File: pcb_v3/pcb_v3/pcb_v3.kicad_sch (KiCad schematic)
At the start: 21 parts, among them J1 Conn_01x05_Socket, J2 Conn_01x04_Pin, J3 Conn_01x04_Socket, U10 TCRT5000, U11 TCRT5000, U2 ULN2003A, U3 NODEMCU-32S, U4 TCRT5000, U5 TCRT5000, U6 TCRT5000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

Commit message: done all footprint
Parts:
- J2: footprint (none) -> Connector_PinHeader_2.54mm:PinHeader_1x04_P2.54mm_Vertical
- J3: footprint (none) -> Connector_PinSocket_2.54mm:PinSocket_1x04_P2.54mm_Vertical
- U2: footprint (none) -> Package_DIP:DIP-16_W7.62mm
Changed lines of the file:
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@@
 			)
 		)
-		(property "Footprint" ""
+		(property "Footprint" "Connector_PinSocket_2.54mm:PinSocket_1x04_P2.54mm_Vertical"
 			(at 99.06 38.1 0)
 			(hide yes)
@@
 			)
 		)
-		(property "Footprint" ""
+		(property "Footprint" "Package_DIP:DIP-16_W7.62mm"
 			(at 54.61 184.15 0)
 			(hide yes)
@@
 			)
 		)
-		(property "Footprint" ""
+		(property "Footprint" "Connector_PinHeader_2.54mm:PinHeader_1x04_P2.54mm_Vertical"
 			(at 121.92 116.84 0)
 			(hide yes)

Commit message: wrong tcrt wiring
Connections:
- net R_U10: now also U10.A; no longer U10.COLL
- net R_U11: now also U11.A; no longer U11.COLL
- net R_U4: now also U4.A; no longer U4.COLL
- net R_U5: now also U5.A; no longer U5.COLL
- net R_U6: now also U6.A; no longer U6.COLL
- net R_U7: now also U7.A; no longer U7.COLL
- net R_U8: now also U8.A; no longer U8.COLL
- net R_U9: now also U9.A; no longer U9.COLL
- net U10_MUXc6: now also U10.COLL; no longer U10.A
- net U11_MUXc7: now also U11.COLL; no longer U11.A
- net U4_MUXc0: now also U4.COLL; no longer U4.A
- net U5_MUXc1: now also U5.COLL; no longer U5.A
- net U6_MUXc2: now also U6.COLL; no longer U6.A
- net U7_MUXc3: now also U7.COLL; no longer U7.A
- net U8_MUXc4: now also U8.COLL; no longer U8.A
- net U9_MUXc5: now also U9.COLL; no longer U9.A

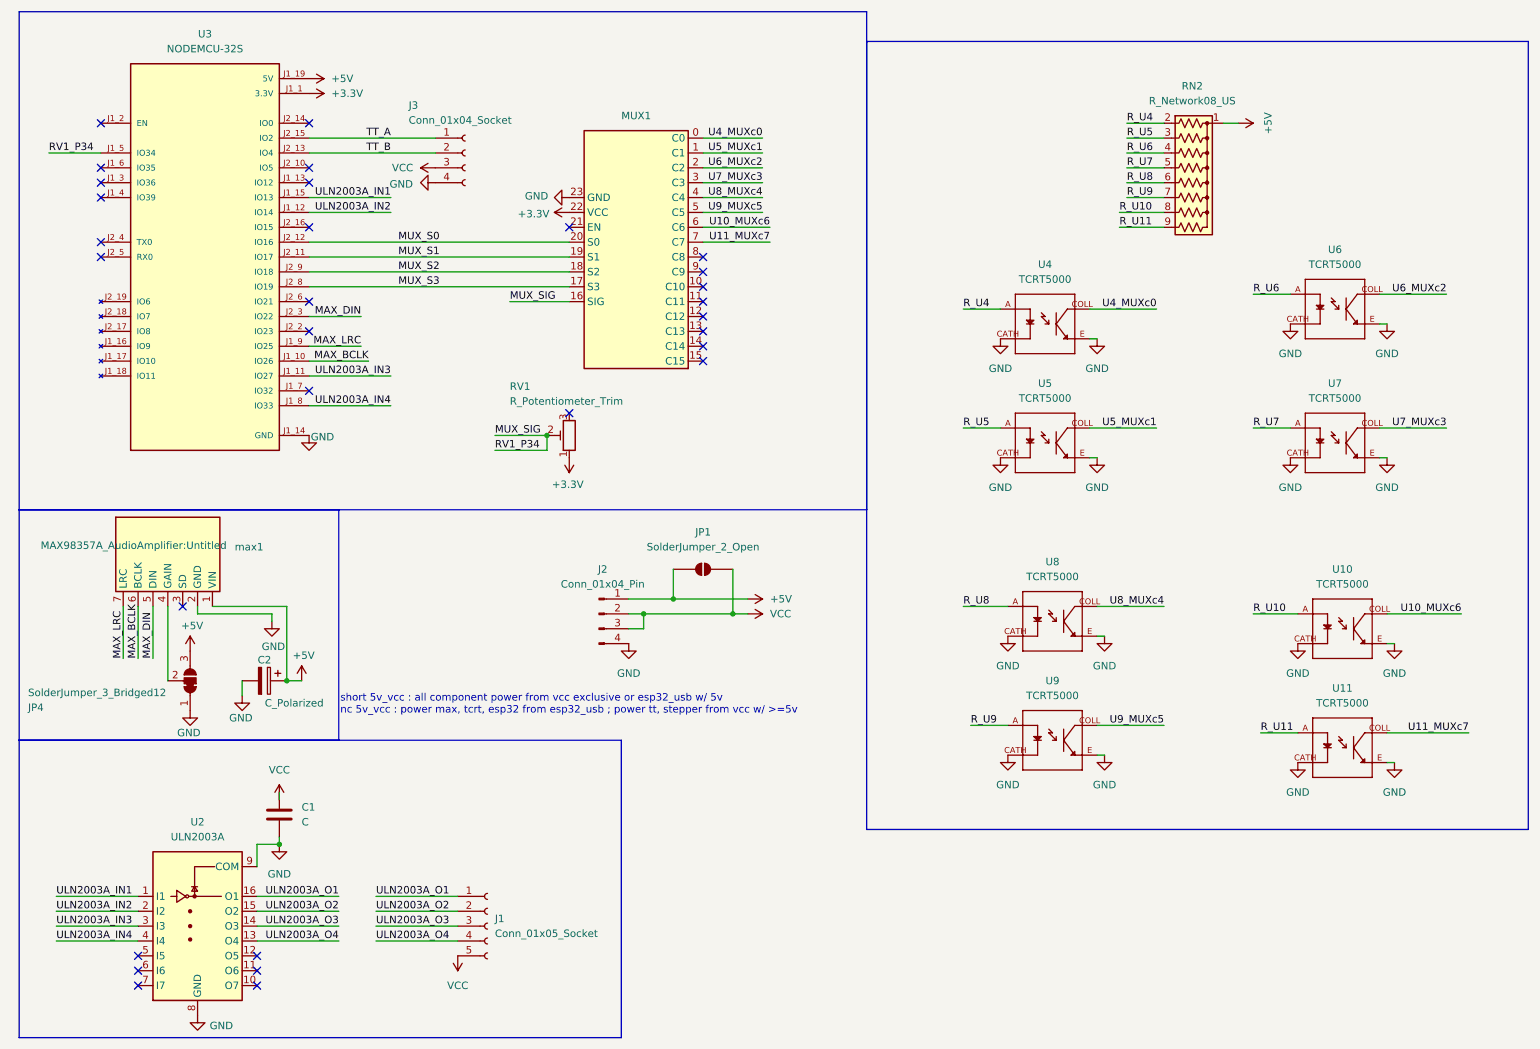
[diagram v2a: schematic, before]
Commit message: 1.delete useless pins in sch and layout 2.rewire potentiometer to vcc, enable us to modify voltage input for motor, preventing fast-battery run out. original wire(mux_sig) is now wired to 3.3v 3.pin9 on uln2003a is now wired to vcc, which previously wired to ground and cause short circuit 4.layout of 2pin power connecter is now modified to a 5mm spaceing module, let us connect power without any soldering on the wire of the battery socket --followings are suggest by seniors 5.jumper is now modify to _3_open , and useing a bigger pad ----todo 6.unify the size of pads on every holes 7.make the wire that crosses the motor socket to uln2003a wider
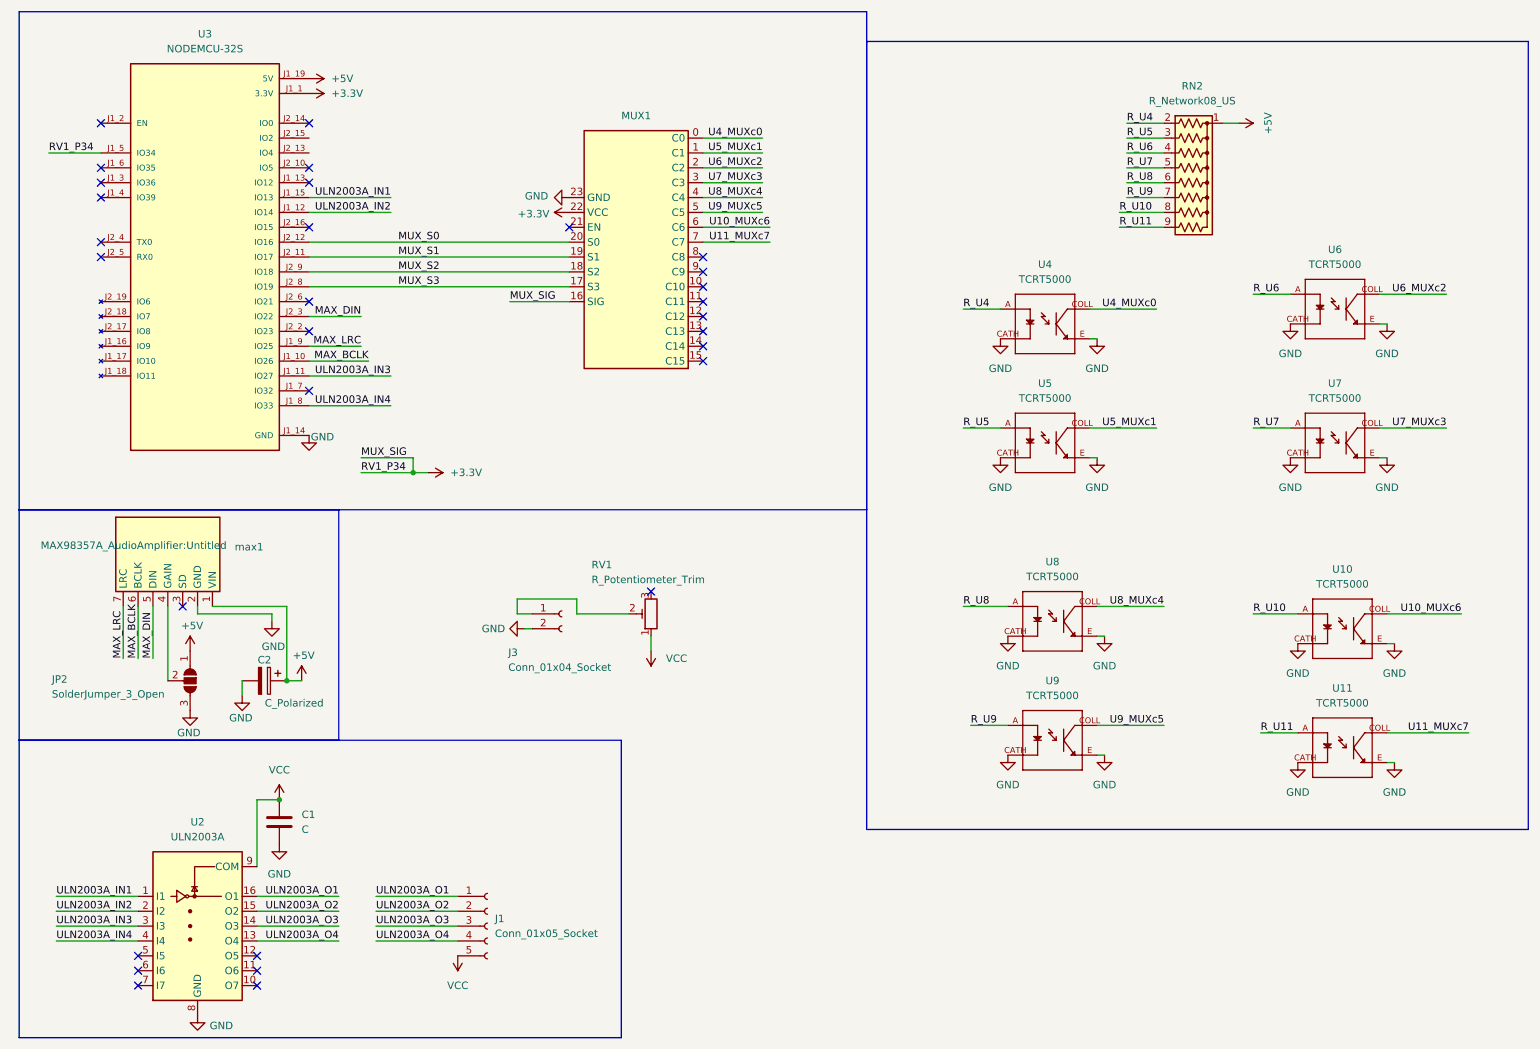
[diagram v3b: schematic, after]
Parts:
- removed J2: Conn_01x04_Pin, Connector_PinHeader_2.54mm:PinHeader_1x04_P2.54mm_Vertical, symbol Connector:Conn_01x04_Pin
- removed JP1: SolderJumper_2_Open, Jumper:SolderJumper-2_P1.3mm_Open_RoundedPad1.0x1.5mm, symbol Jumper:SolderJumper_2_Open
- removed JP4: SolderJumper_3_Bridged12, Jumper:SolderJumper-3_P1.3mm_Bridged12_RoundedPad1.0x1.5mm, symbol Jumper:SolderJumper_3_Bridged12
- added JP2: SolderJumper_3_Open, Jumper:SolderJumper-3_P2.0mm_Open_TrianglePad1.0x1.5mm_NumberLabels, symbol Jumper:SolderJumper_3_Open
- J3: symbol Connector:Conn_01x04_Socket -> Connector:Conn_01x02_Socket
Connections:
- net +3.3V: now also MUX1.16 (SIG), U3.J1_5 (IO34); no longer RV1.1
- net +5V: now also JP2.1 (A)
- net GND: now also J3.2 (Pin_2), JP2.3 (B); no longer J3.4 (Pin_4), U2.9 (COM)
- net VCC: now also RV1.1, U2.9 (COM); no longer J3.3 (Pin_3)
- net at max1.4 (GAIN): now also JP2.2 (C)
- removed net MUX_SIG: MUX1.16 (SIG), RV1.2, U3.J1_5 (IO34)
- net TT_A: no longer names the net of J3.1 (Pin_1)
- net TT_A: now also RV1.2; no longer U3.J2_15 (IO2)
- net TT_B: no longer names the net of U3.J2_13 (IO4)
- net TT_B: no longer J3.2 (Pin_2)
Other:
- note removed: "short 5v_vcc : all component power from vcc exclusive or esp32_usb w/ 5v nc 5v_vcc : power max, tcrt, esp32 from esp32_usb ; power tt, stepper from vcc w/ >=5v"
- moved on the sheet: C1, RV1

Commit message: 1.linbf said tcrt Collector needs a 440ohm res., so i add a res. 2.i have modify the pads in the pcb to 1.95~2mm (depends on hole spaceing differences in diffierent footprints) and hole to 0.8mm
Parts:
- added R1: R, Resistor_THT:R_Axial_DIN0309_L9.0mm_D3.2mm_P12.70mm_Horizontal, symbol Device:R
- J3: footprint Connector_PinSocket_2.54mm:PinSocket_1x04_P2.54mm_Vertical -> TerminalBlock_Phoenix:TerminalBlock_Phoenix_MKDS-1,5-2_1x02_P5.00mm_Horizontal
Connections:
- net +3.3V: now also R1.2; no longer MUX1.16 (SIG), U3.J1_5 (IO34)
- new net MUX_SIG: MUX1.16 (SIG), R1.1, U3.J1_5 (IO34)
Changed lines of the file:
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@@
 	)
 	(junction
-		(at 67.31 148.59)
+		(at 90.17 92.71)
 		(diameter 0)
 		(color 0 0 0 0)
 	)
 	(junction
-		(at 68.58 128.27)
+		(at 67.31 148.59)
 		(diameter 0)
 		(color 0 0 0 0)
 	)
 	(junction
-		(at 90.17 92.71)
+		(at 68.58 128.27)
 		(diameter 0)
 		(color 0 0 0 0)
@@
 	(wire
 		(pts
+			(xy 101.6 92.71) (xy 106.68 92.71)
+		)
+		(stroke
+			(width 0)
+			(type default)
+		)
+	)
+	(wire
+		(pts
 			(xy 29.21 170.18) (xy 43.18 170.18)
 		)
@@
 	(wire
 		(pts
-			(xy 90.17 92.71) (xy 92.71 92.71)
+			(xy 71.12 128.27) (xy 68.58 128.27)
 		)
 		(stroke
@@
 	(wire
 		(pts
-			(xy 71.12 128.27) (xy 68.58 128.27)
+			(xy 130.81 120.65) (xy 130.81 123.19)
 		)
 		(stroke
@@
 	(wire
 		(pts
-			(xy 130.81 120.65) (xy 130.81 123.19)
+			(xy 212.09 45.72) (xy 218.44 45.72)
 		)
 		(stroke
@@
 	(wire
 		(pts
-			(xy 212.09 45.72) (xy 218.44 45.72)
+			(xy 139.7 48.26) (xy 149.86 48.26)
 		)
 		(stroke
@@
 	(wire
 		(pts
-			(xy 139.7 48.26) (xy 149.86 48.26)
+			(xy 210.82 48.26) (xy 218.44 48.26)
 		)
 		(stroke
@@
 	(wire
 		(pts
-			(xy 210.82 48.26) (xy 218.44 48.26)
+			(xy 205.74 85.09) (xy 217.17 85.09)
 		)
 		(stroke
@@
 	(wire
 		(pts
-			(xy 205.74 85.09) (xy 217.17 85.09)
+			(xy 255.27 67.31) (xy 256.54 67.31)
 		)
 		(stroke
@@
 	(wire
 		(pts
-			(xy 255.27 67.31) (xy 256.54 67.31)
+			(xy 90.17 92.71) (xy 93.98 92.71)
 		)
 		(stroke
@@
 			)
 		)
-		(property "Footprint" "Connector_PinSocket_2.54mm:PinSocket_1x04_P2.54mm_Vertical"
+		(property "Footprint" "TerminalBlock_Phoenix:TerminalBlock_Phoenix_MKDS-1,5-2_1x02_P5.00mm_Horizontal"
 			(at 115.57 116.84 0)
 			(hide yes)
@@
 	)
 	(symbol
+		(lib_id "Device:R")
+		(at 97.79 92.71 90)
+		(unit 1)
+		(body_style 1)
+		(exclude_from_sim no)
+		(in_bom yes)
+		(on_board yes)
+		(in_pos_files yes)
+		(dnp no)
+		(fields_autoplaced yes)
+		(property "Reference" "R1"
+			(at 97.79 86.36 90)
+			(show_name no)
+			(do_not_autoplace no)
+			(effects
+				(font
+					(size 1.27 1.27)
+				)
+			)
+		)
+		(property "Value" "R"
+			(at 97.79 88.9 90)
+			(show_name no)
+			(do_not_autoplace no)
+			(effects
+				(font
+					(size 1.27 1.27)
+				)
+			)
+		)
+		(property "Footprint" "Resistor_THT:R_Axial_DIN0309_L9.0mm_D3.2mm_P12.70mm_Horizontal"
+			(at 97.79 94.488 90)
+			(hide yes)
+			(show_name no)
+			(do_not_autoplace no)
+			(effects
+				(font
+					(size 1.27 1.27)
+				)
+			)
+		)
+		(property "Datasheet" ""
+			(at 97.79 92.71 0)
+			(hide yes)
+			(show_name no)
+			(do_not_autoplace no)
+			(effects
+				(font
+					(size 1.27 1.27)
+				)
+			)
+		)
+		(property "Description" "Resistor"
+			(at 97.79 92.71 0)
+			(hide yes)
+			(show_name no)
+			(do_not_autoplace no)
+			(effects
+				(font
+					(size 1.27 1.27)
+				)
+			)
+		)
+		(pin "1"
+		)
+		(pin "2"
+		)
+		(instances
+			(project "pcb_v3"
+				(path "/77ec6267-f937-435f-8f7a-86540cc589d9"
+					(reference "R1")
+					(unit 1)
+				)
+			)
+		)
+	)
+	(symbol
 		(lib_id "TCRT5000:TCRT5000")
 		(at 198.12 87.63 0)
@@
 	(symbol
 		(lib_id "power:+3.3V")
-		(at 92.71 92.71 270)
+		(at 106.68 92.71 270)
 		(unit 1)
 		(body_style 1)
@@
 		(fields_autoplaced yes)
 		(property "Reference" "#PWR022"
-			(at 88.9 92.71 0)
+			(at 102.87 92.71 0)
 			(hide yes)
 			(show_name no)
@@
 		)
 		(property "Value" "+3.3V"
-			(at 96.52 92.7099 90)
+			(at 110.49 92.7099 90)
 			(show_name no)
 			(do_not_autoplace no)
@@
 		)
 		(property "Footprint" ""
-			(at 92.71 92.71 0)
+			(at 106.68 92.71 0)
 			(hide yes)
 			(show_name no)
@@
 		)
 		(property "Datasheet" ""
-			(at 92.71 92.71 0)
+			(at 106.68 92.71 0)
 			(hide yes)
 			(show_name no)
@@
 		)
 		(property "Description" "Power symbol creates a global label with name \"+3.3V\""
-			(at 92.71 92.71 0)
+			(at 106.68 92.71 0)
 			(hide yes)
 			(show_name no)
